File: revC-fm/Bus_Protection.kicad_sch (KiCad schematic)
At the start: 2 parts, among them Q71 MMBT3904T

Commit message: updated fab files
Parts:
- Q71: Manufacturer (none) -> Diodes Incorporated
- R159: renamed from R67; Manufacturer (none) -> Stackpole Electronics; Mfr. Part No (none) -> RMCF0402FT10K0
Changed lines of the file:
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@@
   (symbol (lib_id "Device:R_US") (at 177.8 135.89 270) (unit 1)
     (in_bom yes) (on_board yes) (dnp no)
-    (property "Reference" "R67" (at 177.8 130.683 90)
+    (property "Reference" "R159" (at 177.8 130.683 90)
       (effects (font (size 1.27 1.27)))
     )
@@
       (effects (font (size 1.27 1.27)) hide)
     )
-    (property "Mfr. Part No" "" (at 177.8 135.89 0)
+    (property "Mfr. Part No" "RMCF0402FT10K0" (at 177.8 135.89 0)
+      (effects (font (size 1.27 1.27)) hide)
+    )
+    (property "Manufacturer" "Stackpole Electronics" (at 177.8 135.89 0)
       (effects (font (size 1.27 1.27)) hide)
     )
@@
       (project "mainboard"
         (path "/d1441985-7b63-4bf8-a06d-c70da2e3b78b/00000000-0000-0000-0000-00005ede7915"
-          (reference "R67") (unit 1)
+          (reference "R159") (unit 1)
         )
       )
@@
       (effects (font (size 1.27 1.27)) hide)
     )
+    (property "Manufacturer" "Diodes Incorporated" (at 186.69 135.89 0)
+      (effects (font (size 1.27 1.27)) hide)
+    )
     (pin "1")
     (pin "2")
@@
         )
         (path "/d1441985-7b63-4bf8-a06d-c70da2e3b78b/00000000-0000-0000-0000-00005ede7915"
-          (reference "Q11") (unit 1)
+          (reference "Q39") (unit 1)
         )
       )
@@
   (symbol (lib_id "power:GND") (at 189.23 140.97 0) (unit 1)
     (in_bom yes) (on_board yes) (dnp no)
-    (property "Reference" "#PWR090" (at 189.23 147.32 0)
+    (property "Reference" "#PWR0144" (at 189.23 147.32 0)
       (effects (font (size 1.27 1.27)) hide)
     )
@@
       (project "mainboard"
         (path "/d1441985-7b63-4bf8-a06d-c70da2e3b78b/00000000-0000-0000-0000-00005ede7915"
-          (reference "#PWR090") (unit 1)
+          (reference "#PWR0144") (unit 1)
         )
       )

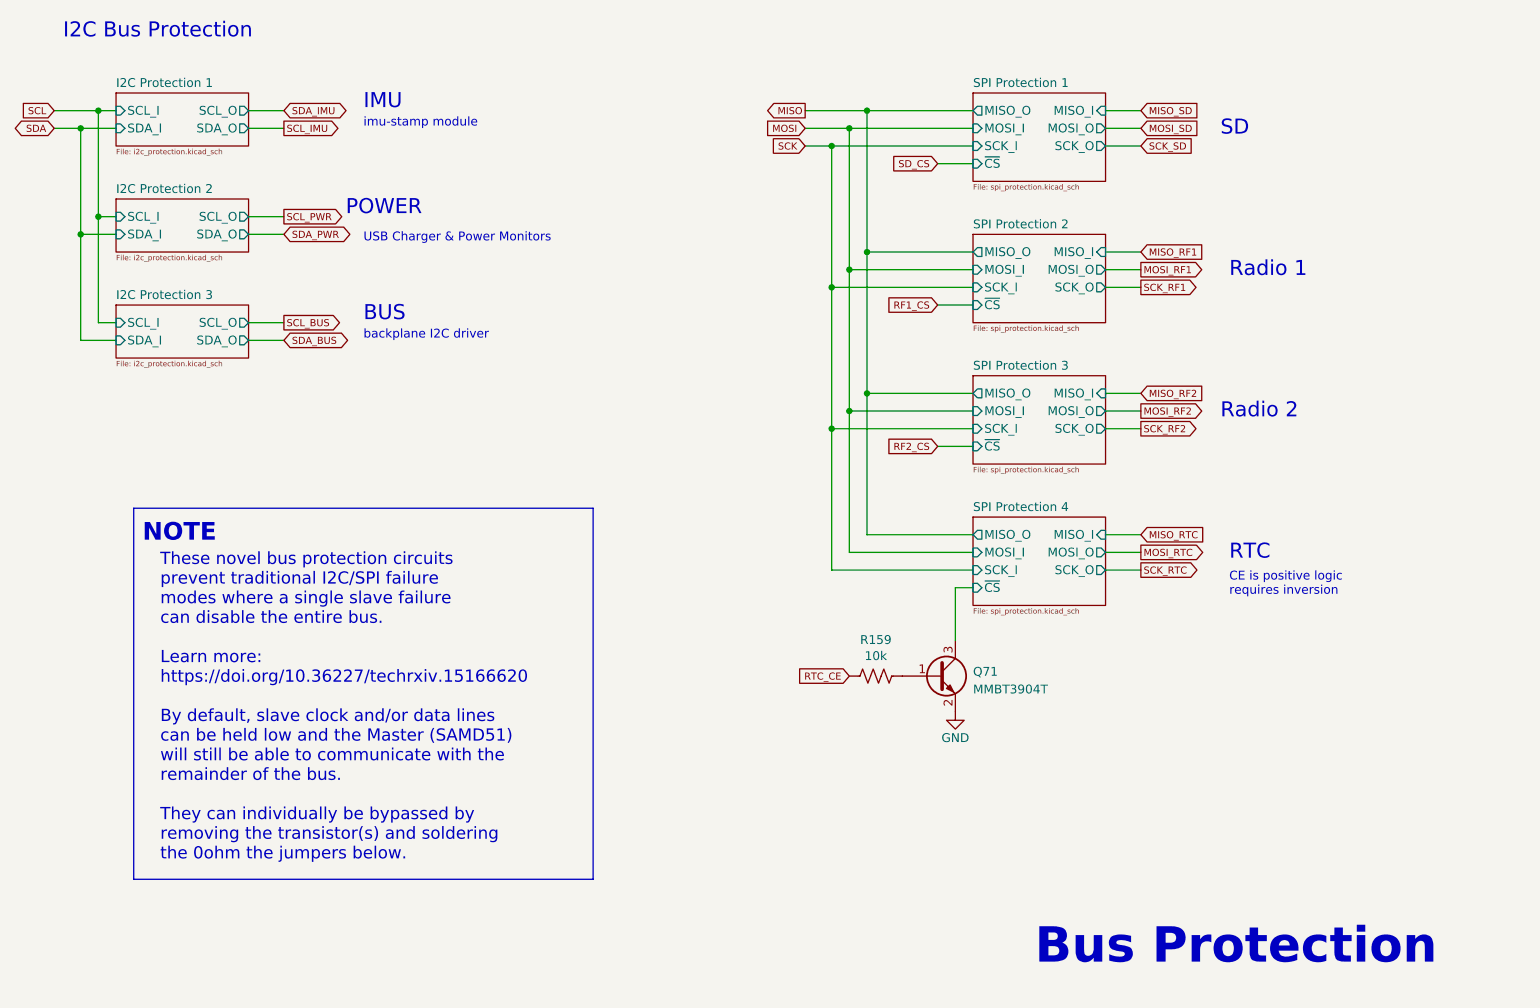
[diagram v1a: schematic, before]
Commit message: updated per review, improved docs
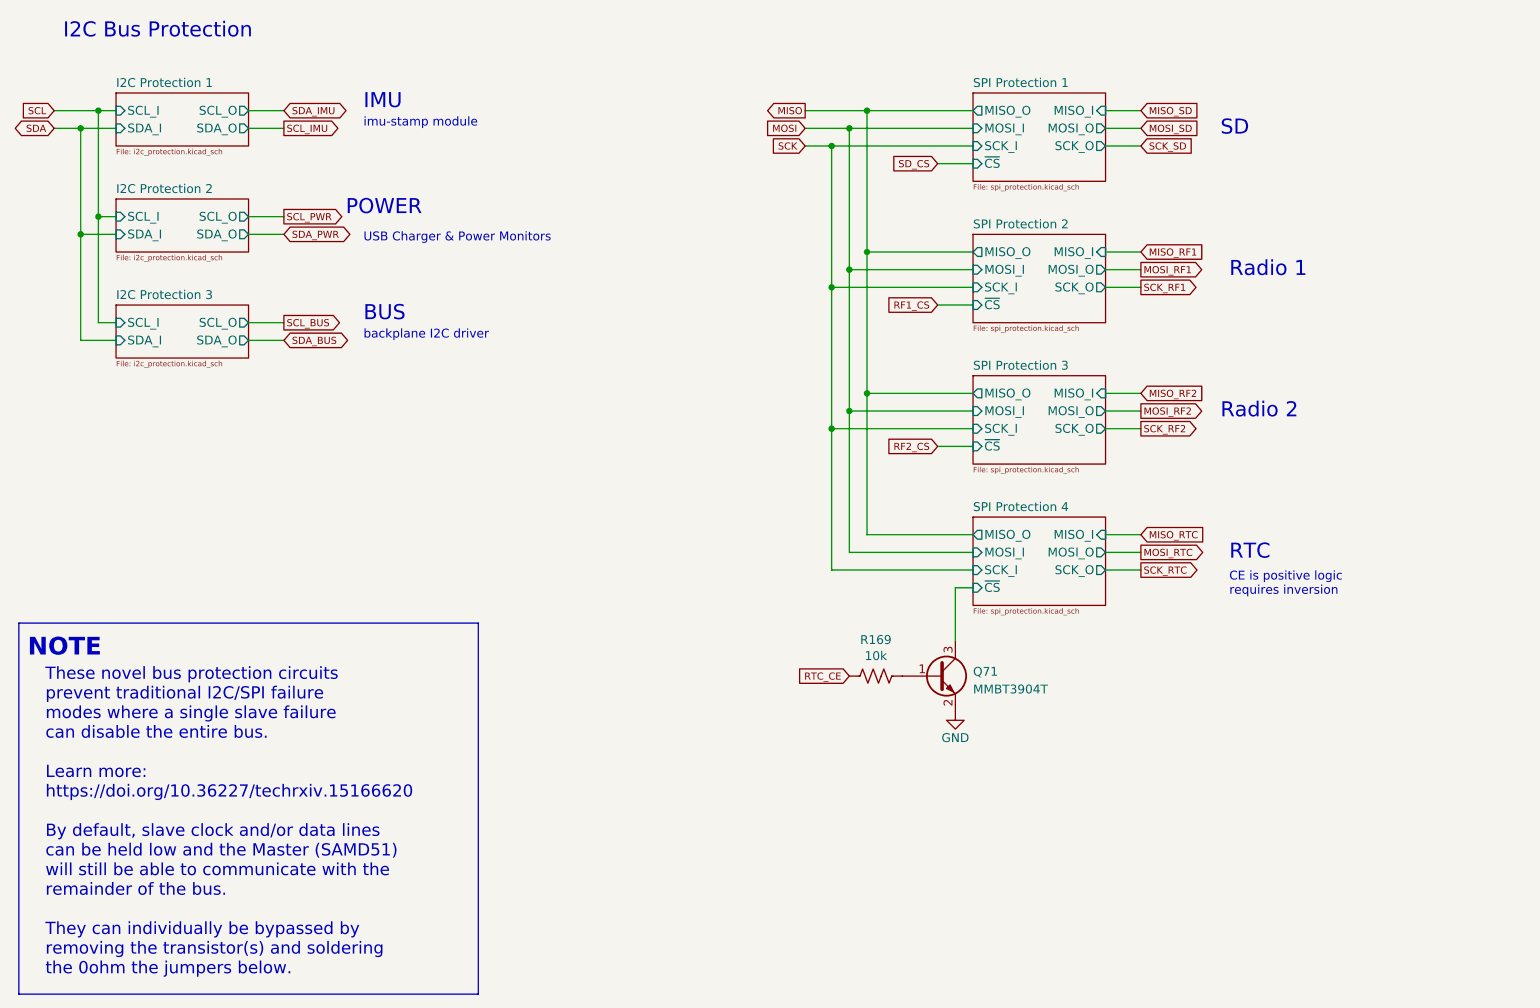
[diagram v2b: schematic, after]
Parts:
- renumbered R159 to R169
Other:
- note removed: "Bus Protection"
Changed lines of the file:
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@@
     (stroke (width 0) (type default))
   )
-  (polyline (pts (xy 71.12 165.1) (xy 137.16 165.1))
+  (polyline (pts (xy 54.61 181.61) (xy 120.65 181.61))
     (stroke (width 0) (type default))
   )
@@
     (stroke (width 0) (type default))
   )
-  (polyline (pts (xy 137.16 165.1) (xy 137.16 111.76))
+  (polyline (pts (xy 120.65 181.61) (xy 120.65 128.27))
     (stroke (width 0) (type default))
   )
@@
     (stroke (width 0) (type default))
   )
-  (polyline (pts (xy 137.16 111.76) (xy 71.12 111.76))
+  (polyline (pts (xy 120.65 128.27) (xy 54.61 128.27))
     (stroke (width 0) (type default))
   )
@@
     (stroke (width 0) (type default))
   )
-  (polyline (pts (xy 71.12 111.76) (xy 71.12 165.1))
+  (polyline (pts (xy 54.61 128.27) (xy 54.61 181.61))
     (stroke (width 0) (type default))
   )
@@
   )
   (text "These novel bus protection circuits\nprevent traditional I2C/SPI failure \nmodes where a single slave failure\ncan disable the entire bus.\n\nLearn more: \nhttps://doi.org/10.36227/techrxiv.15166620\n\nBy default, slave clock and/or data lines \ncan be held low and the Master (SAMD51) \nwill still be able to communicate with the \nremainder of the bus.\n\nThey can individually be bypassed by \nremoving the transistor(s) and soldering\nthe 0ohm the jumpers below."
-    (at 74.93 162.56 0)
+    (at 58.42 179.07 0)
     (effects (font (size 1.7526 1.7526)) (justify left bottom))
   )
@@
     (effects (font (size 1.27 1.27)) (justify left bottom))
   )
-  (text "Bus Protection" (at 200.66 177.8 0)
-    (effects (font (size 5.08 5.08) (thickness 1.016) bold) (justify left bottom))
-  )
-  (text "NOTE" (at 72.39 116.84 0)
+  (text "NOTE" (at 55.88 133.35 0)
     (effects (font (size 2.54 2.54) (thickness 0.508) bold) (justify left bottom))
   )
@@
   (symbol (lib_id "Device:R_US") (at 177.8 135.89 270) (unit 1)
     (in_bom yes) (on_board yes) (dnp no)
-    (property "Reference" "R159" (at 177.8 130.683 90)
+    (property "Reference" "R169" (at 177.8 130.683 90)
       (effects (font (size 1.27 1.27)))
     )
@@
     )
     (property "Manufacturer" "Stackpole Electronics" (at 177.8 135.89 0)
+      (effects (font (size 1.27 1.27)) hide)
+    )
+    (property "Description" "RES 10K OHM 1% 1/16W 0402" (at 177.8 135.89 0)
       (effects (font (size 1.27 1.27)) hide)
     )
@@
       (project "mainboard"
         (path "/d1441985-7b63-4bf8-a06d-c70da2e3b78b/00000000-0000-0000-0000-00005ede7915"
-          (reference "R159") (unit 1)
+          (reference "R169") (unit 1)
         )
       )
@@
     )
     (property "Manufacturer" "Diodes Incorporated" (at 186.69 135.89 0)
+      (effects (font (size 1.27 1.27)) hide)
+    )
+    (property "Description" "TRANS NPN 40V 0.2A SOT523" (at 186.69 135.89 0)
       (effects (font (size 1.27 1.27)) hide)
     )
@@
   (symbol (lib_id "power:GND") (at 189.23 140.97 0) (unit 1)
     (in_bom yes) (on_board yes) (dnp no)
-    (property "Reference" "#PWR0144" (at 189.23 147.32 0)
+    (property "Reference" "#PWR0149" (at 189.23 147.32 0)
       (effects (font (size 1.27 1.27)) hide)
     )
@@
       (project "mainboard"
         (path "/d1441985-7b63-4bf8-a06d-c70da2e3b78b/00000000-0000-0000-0000-00005ede7915"
-          (reference "#PWR0144") (unit 1)
+          (reference "#PWR0149") (unit 1)
         )
       )
